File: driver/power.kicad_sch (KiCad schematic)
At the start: 4 parts

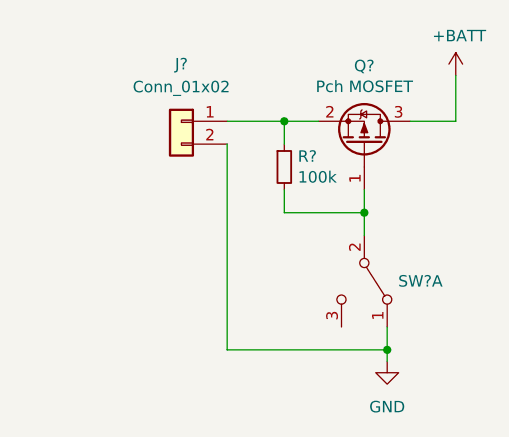
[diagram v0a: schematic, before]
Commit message: 部品配置完了
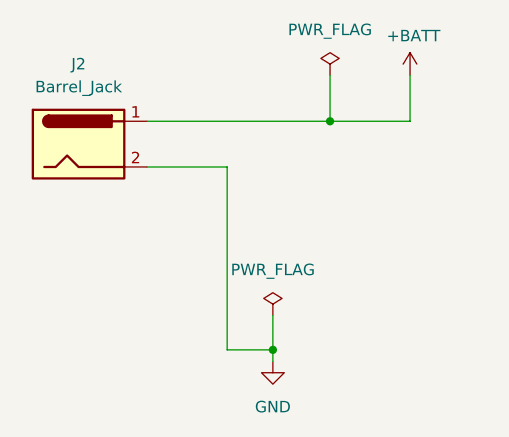
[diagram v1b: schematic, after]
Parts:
- removed J?: Conn_01x02, symbol Connector_Generic:Conn_01x02
- removed Q?: Pch MOSFET, Package_TO_SOT_SMD:SOT-23, symbol Transistor_FET:IRLML6402
- removed R?: 100k, Resistor_SMD:R_0805_2012Metric_Pad1.20x1.40mm_HandSolder, symbol Device:R_Small
- removed SW?: SW_DPDT_x2, My_Device:SlideSwitch, symbol Switch:SW_DPDT_x2
- added J2: Barrel_Jack, Connector_BarrelJack:BarrelJack_Horizontal, symbol Connector:Barrel_Jack
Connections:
- net +BATT: now also J2.1
- net GND: now also J2.2
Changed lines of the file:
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@@
 (kicad_sch (version 20211123) (generator eeschema)
   (paper "A4")
-  (junction (at 154.94 100.33) (diameter 0) (color 0 0 0 0)
+  (junction (at 144.78 115.57) (diameter 0) (color 0 0 0 0)
   )
-  (junction (at 157.48 115.57) (diameter 0) (color 0 0 0 0)
+  (junction (at 151.13 90.17) (diameter 0) (color 0 0 0 0)
   )
-  (junction (at 146.05 90.17) (diameter 0) (color 0 0 0 0)
-  )
-  (wire (pts (xy 160.02 90.17) (xy 165.1 90.17))
+  (wire (pts (xy 130.81 90.17) (xy 151.13 90.17))
     (stroke (width 0) (type default) (color 0 0 0 0))
   )
-  (wire (pts (xy 157.48 116.84) (xy 157.48 115.57))
+  (wire (pts (xy 130.81 95.25) (xy 139.7 95.25))
     (stroke (width 0) (type default) (color 0 0 0 0))
   )
-  (wire (pts (xy 139.7 92.71) (xy 139.7 115.57))
+  (wire (pts (xy 144.78 116.84) (xy 144.78 115.57))
     (stroke (width 0) (type default) (color 0 0 0 0))
   )
-  (wire (pts (xy 139.7 115.57) (xy 157.48 115.57))
+  (wire (pts (xy 139.7 95.25) (xy 139.7 115.57))
     (stroke (width 0) (type default) (color 0 0 0 0))
   )
-  (wire (pts (xy 165.1 90.17) (xy 165.1 85.09))
+  (wire (pts (xy 139.7 115.57) (xy 144.78 115.57))
     (stroke (width 0) (type default) (color 0 0 0 0))
   )
-  (wire (pts (xy 154.94 100.33) (xy 154.94 102.87))
+  (wire (pts (xy 151.13 85.09) (xy 151.13 90.17))
     (stroke (width 0) (type default) (color 0 0 0 0))
   )
-  (wire (pts (xy 146.05 100.33) (xy 154.94 100.33))
+  (wire (pts (xy 160.02 90.17) (xy 160.02 85.09))
     (stroke (width 0) (type default) (color 0 0 0 0))
   )
-  (wire (pts (xy 146.05 97.79) (xy 146.05 100.33))
+  (wire (pts (xy 144.78 111.76) (xy 144.78 115.57))
     (stroke (width 0) (type default) (color 0 0 0 0))
   )
-  (wire (pts (xy 154.94 97.79) (xy 154.94 100.33))
+  (wire (pts (xy 151.13 90.17) (xy 160.02 90.17))
     (stroke (width 0) (type default) (color 0 0 0 0))
   )
-  (wire (pts (xy 146.05 92.71) (xy 146.05 90.17))
-    (stroke (width 0) (type default) (color 0 0 0 0))
-  )
-  (wire (pts (xy 139.7 90.17) (xy 146.05 90.17))
-    (stroke (width 0) (type default) (color 0 0 0 0))
-  )
-  (wire (pts (xy 157.48 115.57) (xy 157.48 113.03))
-    (stroke (width 0) (type default) (color 0 0 0 0))
-  )
-  (wire (pts (xy 146.05 90.17) (xy 149.86 90.17))
-    (stroke (width 0) (type default) (color 0 0 0 0))
-  )
-  (symbol (lib_id "Device:R_Small") (at 146.05 95.25 0) (unit 1)
-    (in_bom yes) (on_board yes)
-    (property "Reference" "R?" (id 0) (at 147.5486 94.0816 0)
-      (effects (font (size 1.27 1.27)) (justify left))
-    )
-    (property "Value" "100k" (id 1) (at 147.5486 96.393 0)
-      (effects (font (size 1.27 1.27)) (justify left))
-    )
-    (property "Footprint" "Resistor_SMD:R_0805_2012Metric_Pad1.20x1.40mm_HandSolder" (id 2) (at 146.05 95.25 0)
+  (symbol (lib_id "power:PWR_FLAG") (at 151.13 85.09 0) (unit 1)
+    (in_bom yes) (on_board yes) (fields_autoplaced)
+    (property "Reference" "#FLG03" (id 0) (at 151.13 83.185 0)
       (effects (font (size 1.27 1.27)) hide)
     )
-    (property "Datasheet" "~" (id 3) (at 146.05 95.25 0)
+    (property "Value" "PWR_FLAG" (id 1) (at 151.13 80.01 0))
+    (property "Footprint" "" (id 2) (at 151.13 85.09 0)
       (effects (font (size 1.27 1.27)) hide)
     )
-    (pin "1")
-    (pin "2")
-  )
-  (symbol (lib_id "power:GND") (at 157.48 116.84 0) (unit 1)
-    (in_bom yes) (on_board yes) (fields_autoplaced)
-    (property "Reference" "#PWR?" (id 0) (at 157.48 123.19 0)
-      (effects (font (size 1.27 1.27)) hide)
-    )
-    (property "Value" "GND" (id 1) (at 157.48 121.92 0))
-    (property "Footprint" "" (id 2) (at 157.48 116.84 0)
-      (effects (font (size 1.27 1.27)) hide)
-    )
-    (property "Datasheet" "" (id 3) (at 157.48 116.84 0)
+    (property "Datasheet" "~" (id 3) (at 151.13 85.09 0)
       (effects (font (size 1.27 1.27)) hide)
     )
     (pin "1")
   )
-  (symbol (lib_id "Transistor_FET:IRLML6402") (at 154.94 92.71 270) (mirror x) (unit 1)
-    (in_bom yes) (on_board yes)
-    (property "Reference" "Q?" (id 0) (at 154.94 84.0232 90))
-    (property "Value" "Pch MOSFET" (id 1) (at 154.94 86.3346 90))
-    (property "Footprint" "Package_TO_SOT_SMD:SOT-23" (id 2) (at 153.035 87.63 0)
-      (effects (font (size 1.27 1.27) italic) (justify left) hide)
-    )
-    (property "Datasheet" "https://www.infineon.com/dgdl/irlml6402pbf.pdf?fileId=5546d462533600a401535668d5c2263c" (id 3) (at 154.94 92.71 0)
-      (effects (font (size 1.27 1.27)) (justify left) hide)
-    )
-    (pin "1")
-    (pin "2")
-    (pin "3")
-  )
-  (symbol (lib_id "Switch:SW_DPDT_x2") (at 154.94 107.95 270) (unit 1)
-    (in_bom yes) (on_board yes)
-    (property "Reference" "SW?" (id 0) (at 158.6992 107.95 90)
-      (effects (font (size 1.27 1.27)) (justify left))
-    )
-    (property "Value" "SW_DPDT_x2" (id 1) (at 158.6992 109.093 90)
-      (effects (font (size 1.27 1.27)) (justify left) hide)
-    )
-    (property "Footprint" "My_Device:SlideSwitch" (id 2) (at 154.94 107.95 0)
+  (symbol (lib_id "power:GND") (at 144.78 116.84 0) (unit 1)
+    (in_bom yes) (on_board yes) (fields_autoplaced)
+    (property "Reference" "#PWR022" (id 0) (at 144.78 123.19 0)
       (effects (font (size 1.27 1.27)) hide)
     )
-    (property "Datasheet" "~" (id 3) (at 154.94 107.95 0)
+    (property "Value" "GND" (id 1) (at 144.78 121.92 0))
+    (property "Footprint" "" (id 2) (at 144.78 116.84 0)
       (effects (font (size 1.27 1.27)) hide)
     )
-    (pin "1")
-    (pin "2")
-    (pin "3")
-    (pin "4")
-    (pin "5")
-    (pin "6")
-  )
-  (symbol (lib_id "power:+BATT") (at 165.1 85.09 0) (unit 1)
-    (in_bom yes) (on_board yes)
-    (property "Reference" "#PWR?" (id 0) (at 165.1 88.9 0)
-      (effects (font (size 1.27 1.27)) hide)
-    )
-    (property "Value" "+BATT" (id 1) (at 165.481 80.6958 0))
-    (property "Footprint" "" (id 2) (at 165.1 85.09 0)
-      (effects (font (size 1.27 1.27)) hide)
-    )
-    (property "Datasheet" "" (id 3) (at 165.1 85.09 0)
+    (property "Datasheet" "" (id 3) (at 144.78 116.84 0)
       (effects (font (size 1.27 1.27)) hide)
     )
     (pin "1")
   )
-  (symbol (lib_id "Connector_Generic:Conn_01x02") (at 134.62 90.17 0) (mirror y) (unit 1)
+  (symbol (lib_id "power:PWR_FLAG") (at 144.78 111.76 0) (unit 1)
     (in_bom yes) (on_board yes) (fields_autoplaced)
-    (property "Reference" "J?" (id 0) (at 134.62 83.82 0))
-    (property "Value" "Conn_01x02" (id 1) (at 134.62 86.36 0))
-    (property "Footprint" "" (id 2) (at 134.62 90.17 0)
+    (property "Reference" "#FLG02" (id 0) (at 144.78 109.855 0)
       (effects (font (size 1.27 1.27)) hide)
     )
-    (property "Datasheet" "~" (id 3) (at 134.62 90.17 0)
+    (property "Value" "PWR_FLAG" (id 1) (at 144.78 106.68 0))
+    (property "Footprint" "" (id 2) (at 144.78 111.76 0)
       (effects (font (size 1.27 1.27)) hide)
     )
+    (property "Datasheet" "~" (id 3) (at 144.78 111.76 0)
+      (effects (font (size 1.27 1.27)) hide)
+    )
+    (pin "1")
+  )
+  (symbol (lib_id "power:+BATT") (at 160.02 85.09 0) (unit 1)
+    (in_bom yes) (on_board yes)
+    (property "Reference" "#PWR023" (id 0) (at 160.02 88.9 0)
+      (effects (font (size 1.27 1.27)) hide)
+    )
+    (property "Value" "+BATT" (id 1) (at 160.401 80.6958 0))
+    (property "Footprint" "" (id 2) (at 160.02 85.09 0)
+      (effects (font (size 1.27 1.27)) hide)
+    )
+    (property "Datasheet" "" (id 3) (at 160.02 85.09 0)
+      (effects (font (size 1.27 1.27)) hide)
+    )
+    (pin "1")
+  )
+  (symbol (lib_id "Connector:Barrel_Jack") (at 123.19 92.71 0) (unit 1)
+    (in_bom yes) (on_board yes) (fields_autoplaced)
+    (property "Reference" "J2" (id 0) (at 123.19 83.82 0))
+    (property "Value" "Barrel_Jack" (id 1) (at 123.19 86.36 0))
+    (property "Footprint" "Connector_BarrelJack:BarrelJack_Horizontal" (id 2) (at 124.46 93.726 0)
+      (effects (font (size 1.27 1.27)) hide)
+    )
+    (property "Datasheet" "~" (id 3) (at 124.46 93.726 0)
+      (effects (font (size 1.27 1.27)) hide)
+    )
